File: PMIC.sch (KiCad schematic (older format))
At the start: 70 parts, among them U4 CSD86330Q3D, U5 LMR62014XMF_NOPB, U6 CSD86330Q3D, U8 TPS65086100

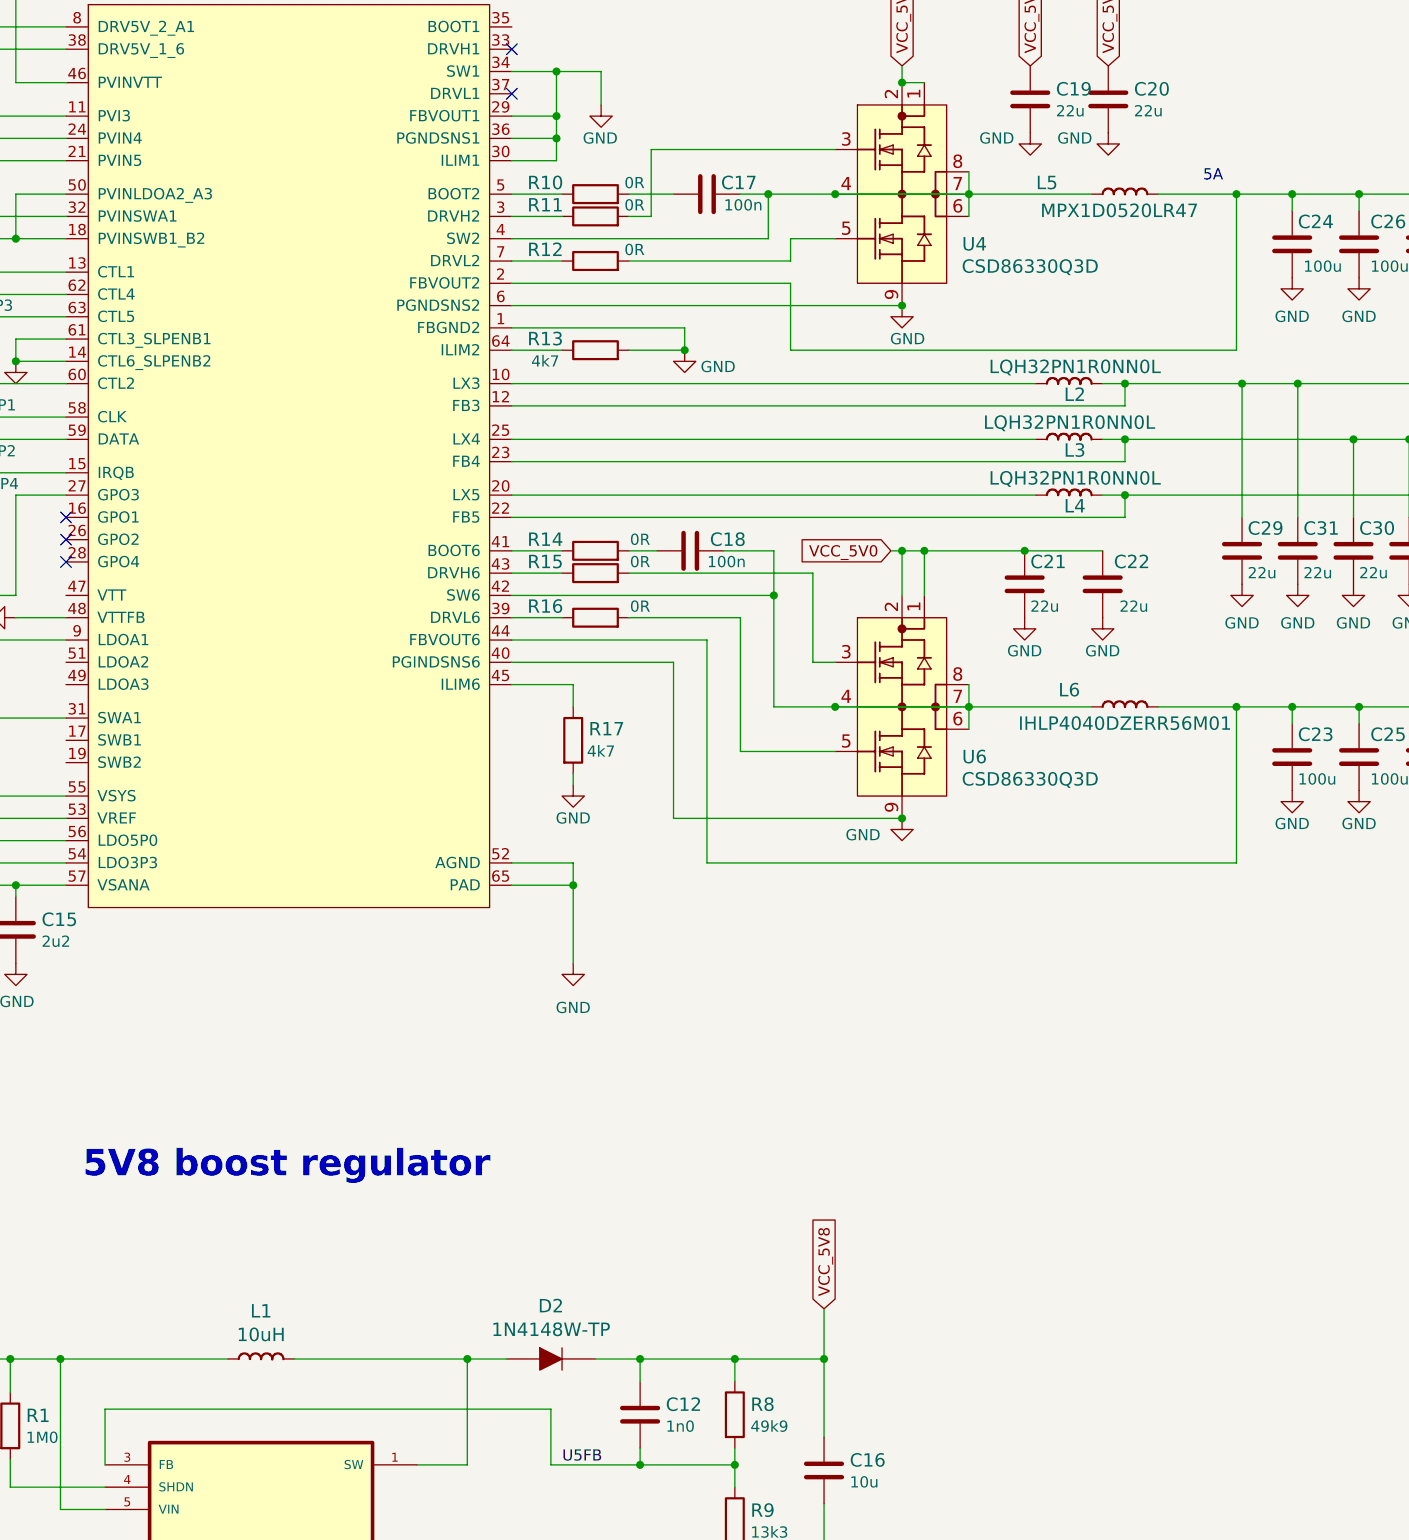
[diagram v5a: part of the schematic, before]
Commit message: Updated PMIC components. PMIC component grouping
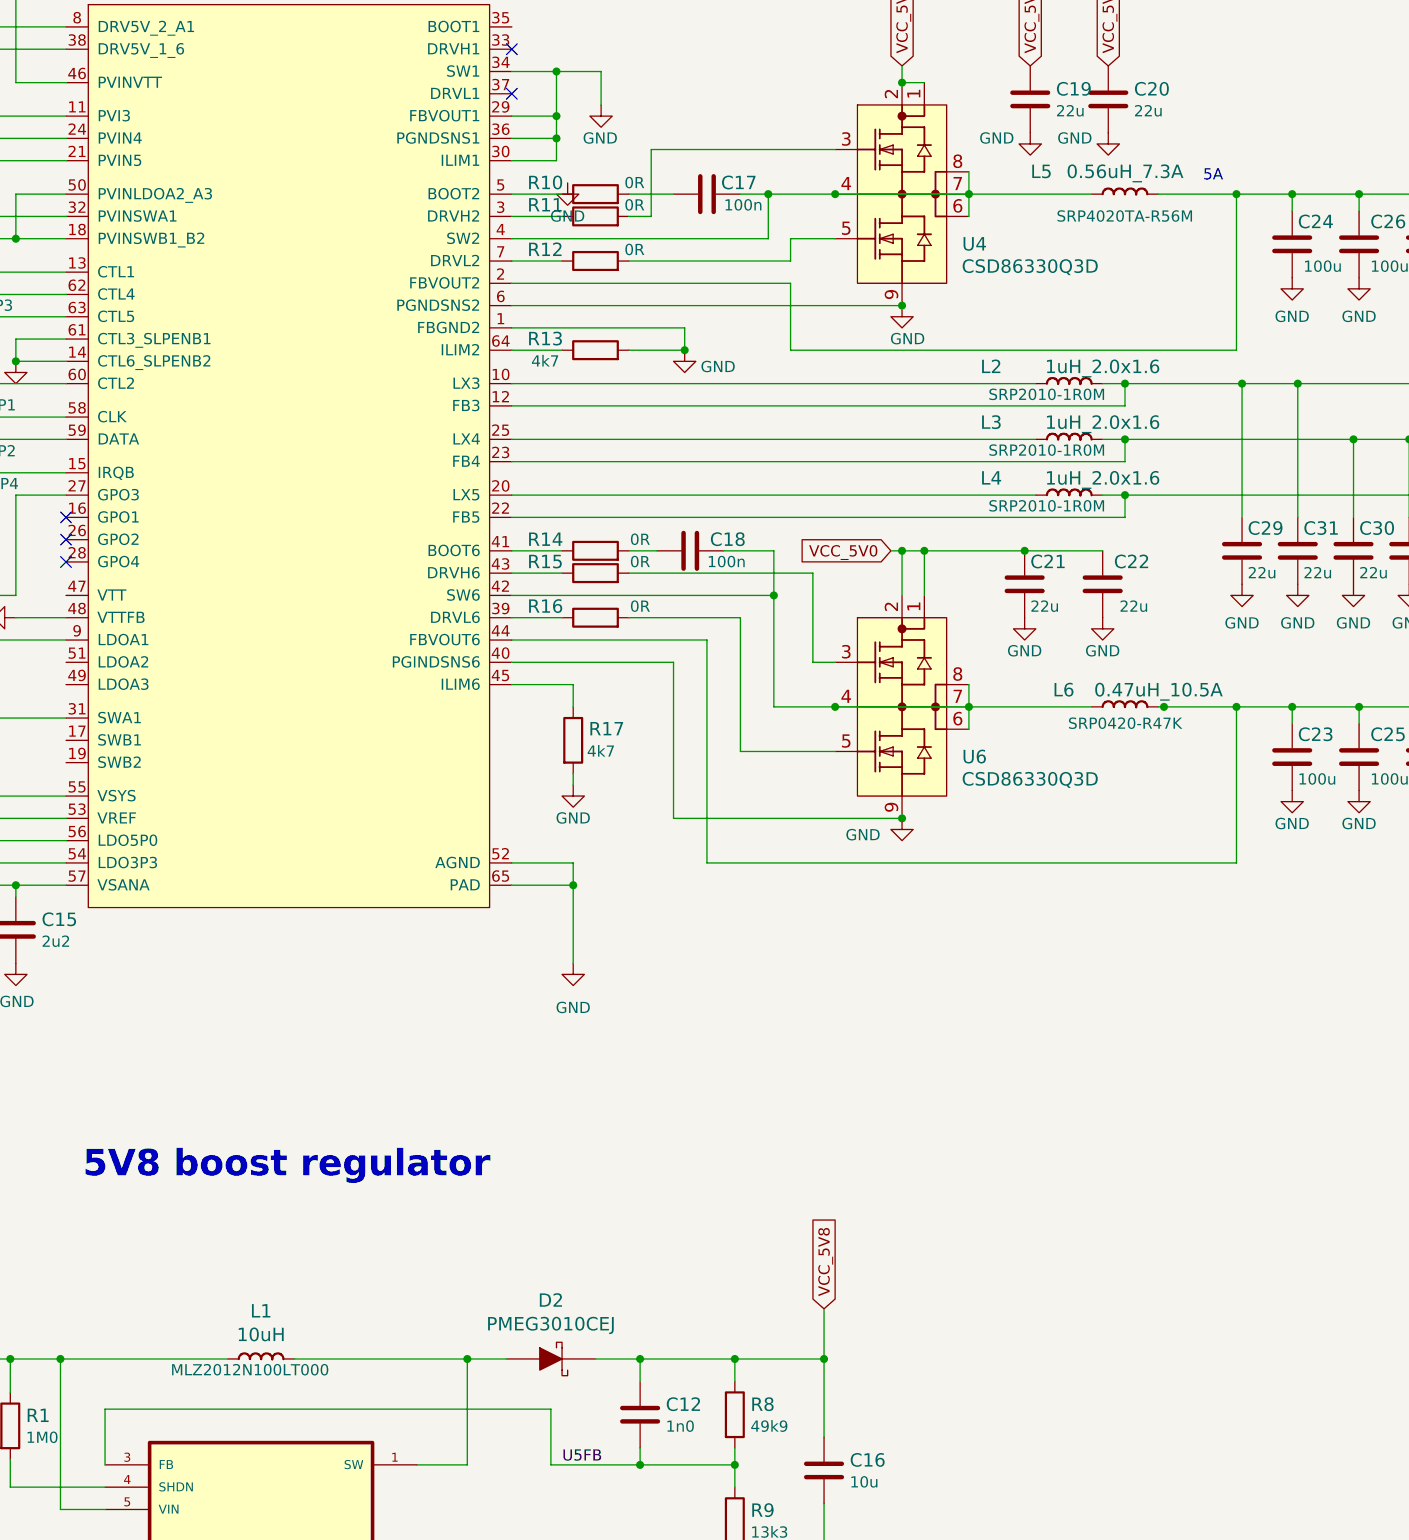
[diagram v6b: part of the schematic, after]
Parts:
- removed D2: 1N4148W-TP, arvsom-footprints:SOD-123, symbol arvsom:1N4148W-TP
- removed L2, L3, L4: LQH32PN1R0NN0L, arvsom-footprints:IND_LQH32PN1R0NN0L, symbol arvsom:LQH32PN1R0NN0L
- removed L5: MPX1D0520LR47, arvsom-footprints:MPX1D0520LR47, symbol arvsom:MPX1D0520LR47
- removed L6: IHLP4040DZERR56M01, arvsom-footprints:IHLP4040DZERR56M01, symbol arvsom:IHLP4040DZERR56M01
- added D2: PMEG3010CEJ, arvsom-footprints:SOD-323F, symbol arvsom:PMEG3010CEJ
- added L2, L3, L4: 1uH_2.0x1.6, arvsom-footprints:INDC2016X100N, symbol arvsom:1uH_2.0x1.6
- added L5: 0.56uH_7.3A, arvsom-footprints:SRP4020, symbol arvsom:0.56uH_7.3A
- added L6: 0.47uH_10.5A, arvsom-footprints:SRP4020, symbol arvsom:0.47uH_10.5A
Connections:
- net VCC_0V9: now also L5.2 (P)
- net VCC_1V1: now also L6.2 (P)
- net VCC_1V2: now also L4.2 (P)
- net VCC_1V8: now also L3.2 (P)
- net VCC_3V3: now also L2.2 (P)
- net VCC_5V8: now also D2.K
- net at U8.10 (LX3): now also L2.1 (P)
- net at U8.20 (LX5): now also L4.1 (P)
- net at U8.25 (LX4): now also L3.1 (P)
- net at C17.2, U4.4 (TGR), U4.6 (VSW)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: now also L5.1 (P)
- net at C18.2, U6.4 (TGR), U6.6 (VSW)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: now also L6.1 (P)
- net at L1.2 (P), U5.1 (SW): now also D2.A
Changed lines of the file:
@@
 Text GLabel 10800 3200 1    50   Input ~ 0
 VCC_5V0
-$Comp
-L arvsom:IHLP4040DZERR56M01 L6
-U 1 1 6092A854
-P 10875 6075
-F 0 "L6" H 10625 6150 60  0000 C CNN
-F 1 "IHLP4040DZERR56M01" H 10875 6000 60  0000 C CNN
-F 2 "arvsom-footprints:IHLP4040DZERR56M01" H 10925 5925 60  0001 C CNN
-F 3 "" H 10930 6105 60  0001 C CNN
-F 4 "Vishay" H 10875 5975 50  0001 C CNN "Manufacturer"
-F 5 "IHLP4040DZERR56M01" H 10875 6176 50  0001 C CNN "MPN"
-	1    10875 6075
-	1    0    0    -1
-$EndComp
 Text GLabel 12875 3775 2    50   Input ~ 0
 VCC_0V9
@@
 Text Notes 12700 4850 0    50   ~ 0
 1A
-$Comp
-L arvsom:LQH32PN1R0NN0L L4
-U 1 1 607B5711
-P 10625 5125
-F 0 "L4" H 10650 5075 60  0000 C CNN
-F 1 "LQH32PN1R0NN0L" H 10650 5200 60  0000 C CNN
-F 2 "arvsom-footprints:IND_LQH32PN1R0NN0L" H 10675 4975 60  0001 C CNN
-F 3 "" H 10680 5155 60  0001 C CNN
-F 4 "Murata" H 10625 5025 50  0001 C CNN "Manufacturer"
-F 5 "LQH32PN1R0NN0L" H 10625 5226 50  0001 C CNN "MPN"
-	1    10625 5125
-	1    0    0    -1
-$EndComp
 Wire Wire Line
 	8125 5125 10475 5125
@@
 Wire Wire Line
 	8125 4875 10475 4875
-$Comp
-L arvsom:LQH32PN1R0NN0L L3
-U 1 1 6076DEAF
-P 10625 4875
-F 0 "L3" H 10650 4825 60  0000 C CNN
-F 1 "LQH32PN1R0NN0L" H 10625 4950 60  0000 C CNN
-F 2 "arvsom-footprints:IND_LQH32PN1R0NN0L" H 10675 4725 60  0001 C CNN
-F 3 "" H 10680 4905 60  0001 C CNN
-F 4 "Murata" H 10625 4775 50  0001 C CNN "Manufacturer"
-F 5 "LQH32PN1R0NN0L" H 10625 4976 50  0001 C CNN "MPN"
-	1    10625 4875
-	1    0    0    -1
-$EndComp
 Wire Wire Line
 	10875 4625 10775 4625
@@
 	8125 4625 10475 4625
 $Comp
-L arvsom:LQH32PN1R0NN0L L2
-U 1 1 6092B106
-P 10625 4625
-F 0 "L2" H 10650 4575 60  0000 C CNN
-F 1 "LQH32PN1R0NN0L" H 10650 4700 60  0000 C CNN
-F 2 "arvsom-footprints:IND_LQH32PN1R0NN0L" H 10675 4475 60  0001 C CNN
-F 3 "" H 10680 4655 60  0001 C CNN
-F 4 "Murata" H 10625 4525 50  0001 C CNN "Manufacturer"
-F 5 "LQH32PN1R0NN0L" H 10625 4726 50  0001 C CNN "MPN"
-	1    10625 4625
-	1    0    0    -1
-$EndComp
-$Comp
 L arvsom:R_0R_0402 R14
 U 1 1 6080F73F
@@
 VCC_5V0
 Wire Wire Line
-	11025 6075 11375 6075
+	11025 6075 11050 6075
 Text GLabel 12875 6075 2    50   Input ~ 0
 VCC_1V1
@@
 Wire Wire Line
 	7925 9475 7925 9000
-$Comp
-L arvsom:10uH L1
-U 1 1 60AE966B
-P 7000 9000
-F 0 "L1" H 7000 9214 60  0000 C CNN
-F 1 "10uH" H 7000 9108 60  0000 C CNN
-F 2 "arvsom-footprints:0805-res" H 7050 8850 60  0001 C CNN
-F 3 "" H 7055 9030 60  0001 C CNN
-F 4 "TDK" H 7000 8900 50  0001 C CNN "Manufacturer"
-F 5 "MLZ2012N100LT000" H 6950 8950 50  0001 C CNN "MPN"
-	1    7000 9000
-	1    0    0    -1
-$EndComp
 Wire Wire Line
 	6100 9000 6850 9000
@@
 	1    0    0    -1
 $EndComp
-$Comp
-L arvsom:1N4148W-TP D2
-U 1 1 60B809B9
-P 8300 9000
-F 0 "D2" H 8300 9237 60  0000 C CNN
-F 1 "1N4148W-TP" H 8300 9131 60  0000 C CNN
-F 2 "arvsom-footprints:SOD-123" H 8500 9200 60  0001 L CNN
-F 3 "https://www.mccsemi.com/pdf/Products/1N4148W(SOD123).pdf" H 8500 9300 60  0001 L CNN
-F 4 "1N4148W-TP" H 8500 9500 60  0001 L CNN "MPN"
-F 5 "Micro Commercial Co" H 8500 10100 60  0001 L CNN "Manufacturer"
-	1    8300 9000
-	1    0    0    -1
-$EndComp
 Wire Wire Line
 	8100 9000 7925 9000
@@
 Wire Wire Line
 	10725 3775 10175 3775
-$Comp
-L arvsom:MPX1D0520LR47 L5
-U 1 1 6092BA13
-P 10875 3775
-F 0 "L5" H 10525 3825 60  0000 C CNN
-F 1 "MPX1D0520LR47" H 10850 3700 60  0000 C CNN
-F 2 "arvsom-footprints:MPX1D0520LR47" H 10925 3625 60  0001 C CNN
-F 3 "" H 10930 3805 60  0001 C CNN
-F 4 "Kemet" H 10875 3675 50  0001 C CNN "Manufacturer"
-F 5 "MPX1D0520LR47" H 10875 3876 50  0001 C CNN "MPN"
-	1    10875 3775
-	1    0    0    -1
-$EndComp
 Wire Wire Line
 	9575 3775 9275 3775
@@
 L arvsom:GND #PWR0127
 U 1 1 609E6360
-P 10425 5675
-F 0 "#PWR0127" H 10425 5425 50  0001 C CNN
-F 1 "GND" H 10425 5525 50  0000 C CNN
-F 2 "" H 10425 5675 50  0001 C CNN
-F 3 "" H 10425 5675 50  0001 C CNN
-	1    10425 5675
+P 8375 3725
+F 0 "#PWR0127" H 8375 3475 50  0001 C CNN
+F 1 "GND" H 8375 3575 50  0000 C CNN
+F 2 "" H 8375 3725 50  0001 C CNN
+F 3 "" H 8375 3725 50  0001 C CNN
+	1    8375 3725
 	1    0    0    -1
 $EndComp
@@
 	9825 5375 9875 5375
 Connection ~ 9875 5375
-Wire Wire Line
-	9975 5375 10425 5375
 Connection ~ 10425 5375
 Wire Wire Line
@@
 Text GLabel 3400 3925 0    50   Input ~ 0
 PWR_OFF
+$Comp
+L arvsom:GND #PWR?
+U 1 1 60A57F5F
+P 10425 5675
+F 0 "#PWR?" H 10425 5425 50  0001 C CNN
+F 1 "GND" H 10425 5525 50  0000 C CNN
+F 2 "" H 10425 5675 50  0001 C CNN
+F 3 "" H 10425 5675 50  0001 C CNN
+	1    10425 5675
+	1    0    0    -1
+$EndComp
+$Comp
+L arvsom:PMEG3010CEJ D2
+U 1 1 60ABAE6A
+P 8300 9000
+F 0 "D2" H 8300 9262 60  0000 C CNN
+F 1 "PMEG3010CEJ" H 8300 9156 60  0000 C CNN
+F 2 "arvsom-footprints:SOD-323F" H 8500 9200 60  0001 L CNN
+F 3 "https://assets.nexperia.com/documents/data-sheet/PMEG3010CEH_PMEG3010CEJ.pdf" H 8500 9300 60  0001 L CNN
+F 4 "PMEG3010CEJ" H 8500 9500 60  0001 L CNN "MPN"
+F 5 "Nexperia" H 8500 10100 60  0001 L CNN "Manufacturer"
+	1    8300 9000
+	1    0    0    -1
+$EndComp
+$Comp
+L arvsom:10uH L1
+U 1 1 60AE966B
+P 7000 9000
+F 0 "L1" H 7000 9214 60  0000 C CNN
+F 1 "10uH" H 7000 9108 60  0000 C CNN
+F 2 "arvsom-footprints:0805-res" H 7050 8850 60  0001 C CNN
+F 3 "" H 7055 9030 60  0001 C CNN
+F 4 "TDK" H 7000 8900 50  0001 C CNN "Manufacturer"
+F 5 "MLZ2012N100LT000" H 6950 8950 50  0000 C CNN "MPN"
+	1    7000 9000
+	1    0    0    -1
+$EndComp
+$Comp
+L arvsom:1uH_2.0x1.6 L2
+U 1 1 60AC873B
+P 10625 4625
+F 0 "L2" H 10275 4700 60  0000 C CNN
+F 1 "1uH_2.0x1.6" H 10775 4700 60  0000 C CNN
+F 2 "arvsom-footprints:INDC2016X100N" H 10675 4475 60  0001 C CNN
+F 3 "https://www.bourns.com/docs/Product-Datasheets/SRP2010.pdf" H 10680 4655 60  0001 C CNN
+F 4 "BOURNS" H 10625 4525 50  0001 C CNN "Manufacturer"
+F 5 "SRP2010-1R0M" H 10525 4575 50  0000 C CNN "MPN"
+	1    10625 4625
+	1    0    0    -1
+$EndComp
+Wire Wire Line
+	9975 5375 10425 5375
+$Comp
+L arvsom:1uH_2.0x1.6 L3
+U 1 1 60AE7DB7
+P 10625 4875
+F 0 "L3" H 10275 4950 60  0000 C CNN
+F 1 "1uH_2.0x1.6" H 10775 4950 60  0000 C CNN
+F 2 "arvsom-footprints:INDC2016X100N" H 10675 4725 60  0001 C CNN
+F 3 "https://www.bourns.com/docs/Product-Datasheets/SRP2010.pdf" H 10680 4905 60  0001 C CNN
+F 4 "BOURNS" H 10625 4775 50  0001 C CNN "Manufacturer"
+F 5 "SRP2010-1R0M" H 10525 4825 50  0000 C CNN "MPN"
+	1    10625 4875
+	1    0    0    -1
+$EndComp
+$Comp
+L arvsom:1uH_2.0x1.6 L4
+U 1 1 60AE8860
+P 10625 5125
+F 0 "L4" H 10275 5200 60  0000 C CNN
+F 1 "1uH_2.0x1.6" H 10775 5200 60  0000 C CNN
+F 2 "arvsom-footprints:INDC2016X100N" H 10675 4975 60  0001 C CNN
+F 3 "https://www.bourns.com/docs/Product-Datasheets/SRP2010.pdf" H 10680 5155 60  0001 C CNN
+F 4 "BOURNS" H 10625 5025 50  0001 C CNN "Manufacturer"
+F 5 "SRP2010-1R0M" H 10525 5075 50  0000 C CNN "MPN"
+	1    10625 5125
+	1    0    0    -1
+$EndComp
+$Comp
+L arvsom:0.56uH_7.3A L5
+U 1 1 60AF2319
+P 10875 3775
+F 0 "L5" H 10500 3875 60  0000 C CNN
+F 1 "0.56uH_7.3A" H 10875 3875 60  0000 C CNN
+F 2 "arvsom-footprints:SRP4020" H 10925 3625 60  0001 C CNN
+F 3 "https://www.bourns.com/docs/Product-Datasheets/SRP4020TA.pdf" H 10930 3805 60  0001 C CNN
+F 4 "BOURNS" H 10875 3675 50  0001 C CNN "Manufacturer"
+F 5 " SRP4020TA-R56M " H 10875 3675 50  0000 C CNN "MPN"
+	1    10875 3775
+	1    0    0    -1
+$EndComp
+$Comp
+L arvsom:0.47uH_10.5A L6
+U 1 1 60AF8EA1
+P 10875 6075
+F 0 "L6" H 10600 6150 60  0000 C CNN
+F 1 "0.47uH_10.5A" H 11025 6150 60  0000 C CNN
+F 2 "arvsom-footprints:SRP4020" H 10925 5925 60  0001 C CNN
+F 3 "https://www.bourns.com/docs/product-datasheets/srp0420.pdf" H 10930 6105 60  0001 C CNN
+F 4 "BOURNS" H 10875 5975 50  0001 C CNN "Manufacturer"
+F 5 " SRP0420-R47K " H 10875 6000 50  0000 C CNN "MPN"
+	1    10875 6075
+	1    0    0    -1
+$EndComp
+Connection ~ 11050 6075
+Wire Wire Line
+	11050 6075 11375 6075
 $EndSCHEMATC

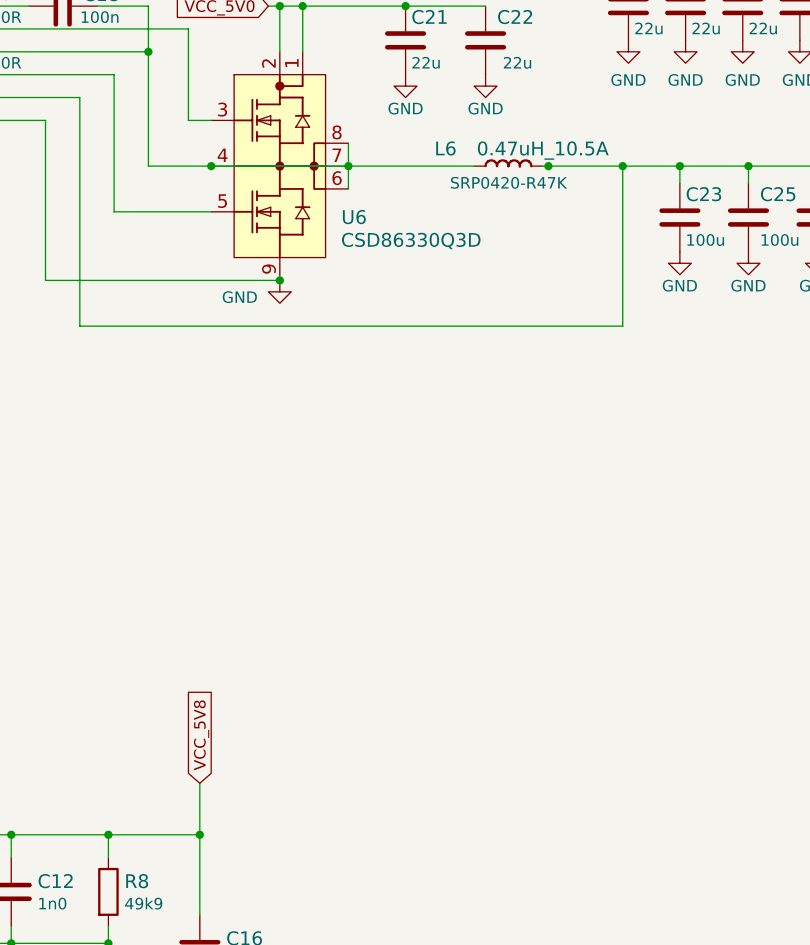
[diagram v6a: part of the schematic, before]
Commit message: PMIC initial placement
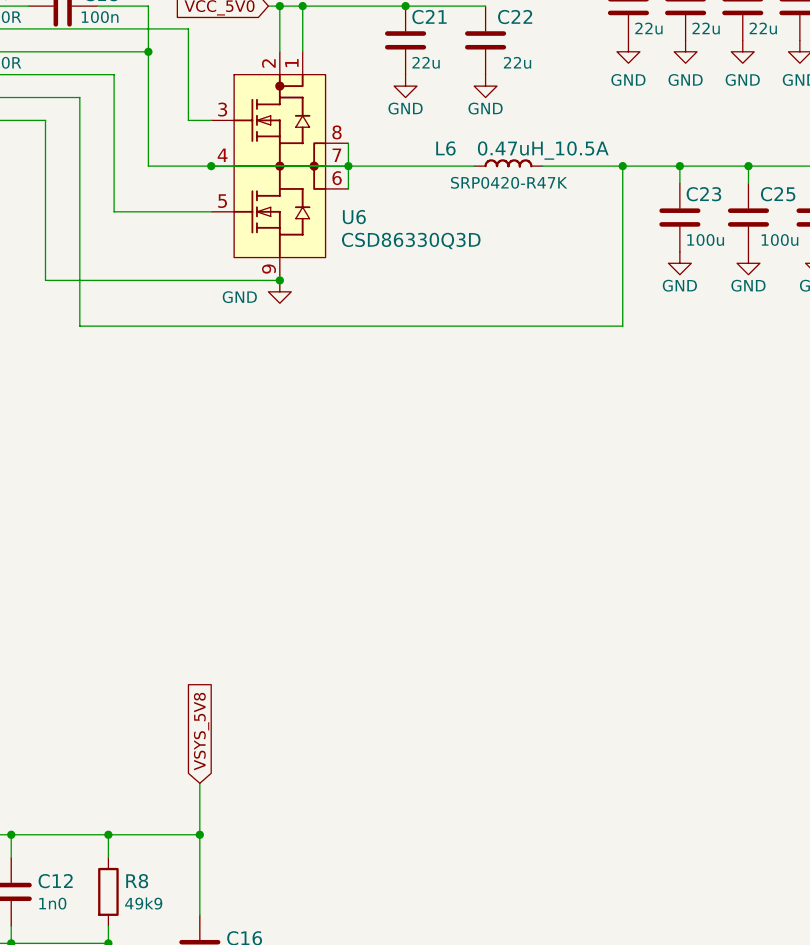
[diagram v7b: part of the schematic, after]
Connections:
- net VCC_5V8 is gone; now on net VSYS_5V8: C12.1, C16.1, D2.K, R8.1
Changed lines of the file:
@@
 Text GLabel 9825 5375 0    50   Input ~ 0
 VCC_5V0
-Wire Wire Line
-	11025 6075 11050 6075
 Text GLabel 12875 6075 2    50   Input ~ 0
 VCC_1V1
@@
 	9525 9000 9525 8775
 Text GLabel 9525 8775 1    50   Input ~ 0
-VCC_5V8
+VSYS_5V8
 Wire Wire Line
 	9125 9000 9525 9000
@@
 PWR_OFF
 $Comp
-L arvsom:GND #PWR?
+L arvsom:GND #PWR0110
 U 1 1 60A57F5F
 P 10425 5675
-F 0 "#PWR?" H 10425 5425 50  0001 C CNN
+F 0 "#PWR0110" H 10425 5425 50  0001 C CNN
 F 1 "GND" H 10425 5525 50  0000 C CNN
 F 2 "" H 10425 5675 50  0001 C CNN
@@
 	1    0    0    -1
 $EndComp
-Connection ~ 11050 6075
 Wire Wire Line
-	11050 6075 11375 6075
+	11025 6075 11375 6075
 $EndSCHEMATC
